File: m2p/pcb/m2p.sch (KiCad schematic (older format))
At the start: 102 parts, among them IC1 APU1205-HF-3, IC2 ADuM1201, IC3 SP100-2T, IC4 ADXL375, IC5 STM32F303C, P1 CONN_2, P2 CONN_2, P3 CONN_4, P4 CONN_2, P5 SWD, P6 CONN_2, P7 CONN_2, Q1 MOSFET_P, Q2 MOSFET_P, Q3 MOSFET_N, Q4 MOSFET_N, U1 BAT BOX, U2 ARM SW, U3 RG LED, X1 8M

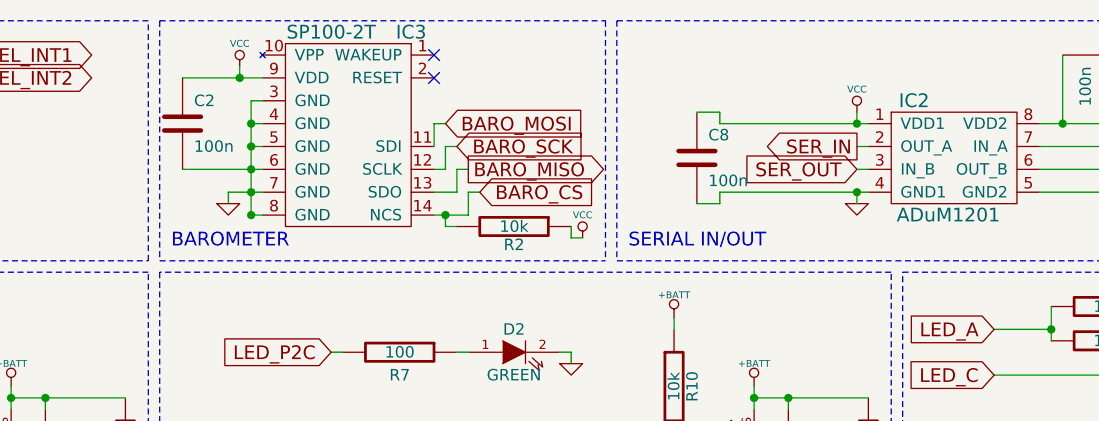
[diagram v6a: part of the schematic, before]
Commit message: swap SP100-2T for MS5611-01BA03 barometer
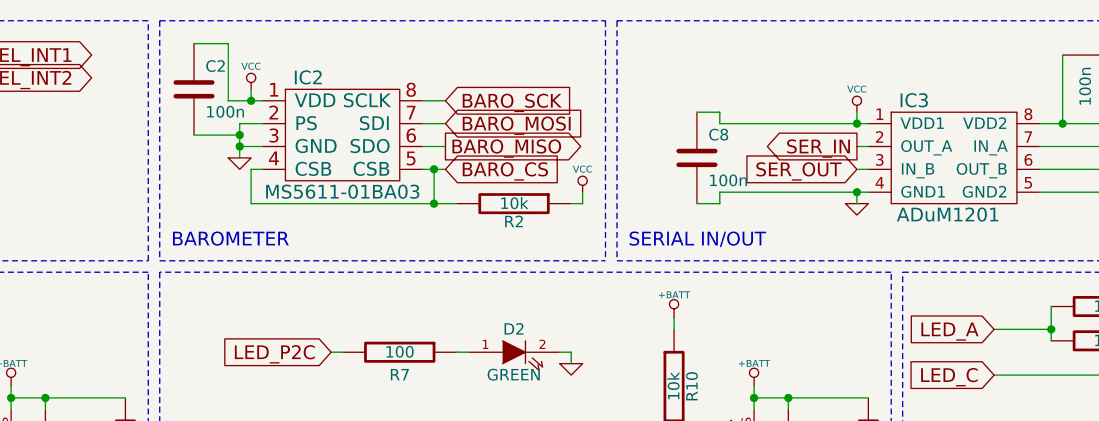
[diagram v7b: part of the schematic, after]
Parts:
- removed IC3: SP100-2T, symbol SP100-2T
- added IC2: MS5611-01BA03, symbol MS5611-01BA03
- renumbered IC2 to IC3
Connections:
- net BARO_CS: now also IC2.4 (CSB), IC2.5 (CSB)
- net BARO_MISO: now also IC2.6 (SDO)
- net BARO_MOSI: now also IC2.7 (SDI)
- net BARO_SCK: now also IC2.8 (SCLK)
- net GND: now also IC2.2 (PS), IC2.3 (GND)
- net VCC: now also IC2.1 (VDD)
- no-connect marks 11 -> 9
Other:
- moved on the sheet: C2, R2
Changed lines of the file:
@@
 LIBS:testpad
 LIBS:stm32f303c
+LIBS:ms5611-01ba03
 LIBS:m2p-cache
 EELAYER 24 0
@@
 $EndComp
 $Comp
-L VCC #PWR5
+L VCC #PWR4
 U 1 1 536844D4
 P 3200 750
-F 0 "#PWR5" H 3200 850 30  0001 C CNN
+F 0 "#PWR4" H 3200 850 30  0001 C CNN
 F 1 "VCC" H 3200 850 30  0000 C CNN
 F 2 "" H 3200 750 60  0001 C CNN
@@
 $EndComp
 $Comp
-L GND #PWR13
+L GND #PWR14
 U 1 1 536844CD
 P 3500 1250
-F 0 "#PWR13" H 3500 1250 30  0001 C CNN
+F 0 "#PWR14" H 3500 1250 30  0001 C CNN
 F 1 "GND" H 3500 1180 30  0001 C CNN
 F 2 "" H 3500 1250 60  0001 C CNN
@@
 $EndComp
 $Comp
-L VCC #PWR19
+L VCC #PWR15
 U 1 1 53683EED
-P 7950 1450
-F 0 "#PWR19" H 7950 1550 30  0001 C CNN
-F 1 "VCC" H 7950 1550 30  0000 C CNN
-F 2 "" H 7950 1450 60  0001 C CNN
-F 3 "" H 7950 1450 60  0001 C CNN
-	1    7950 1450
+P 7950 1250
+F 0 "#PWR15" H 7950 1350 30  0001 C CNN
+F 1 "VCC" H 7950 1350 30  0000 C CNN
+F 2 "" H 7950 1250 60  0001 C CNN
+F 3 "" H 7950 1250 60  0001 C CNN
+	1    7950 1250
 	1    0    0    -1
 $EndComp
@@
 L R R2
 U 1 1 53683ED0
-P 7650 1400
-F 0 "R2" V 7730 1400 50  0000 C CNN
-F 1 "10k" V 7650 1400 50  0000 C CNN
-F 2 "0603" H 7650 1400 60  0001 C CNN
-F 3 "" H 7650 1400 60  0001 C CNN
-F 4 "2332016" V 7650 1400 60  0001 C CNN "Farnell"
-	1    7650 1400
+P 7650 1300
+F 0 "R2" V 7730 1300 50  0000 C CNN
+F 1 "10k" V 7650 1300 50  0000 C CNN
+F 2 "0603" H 7650 1300 60  0001 C CNN
+F 3 "" H 7650 1300 60  0001 C CNN
+F 4 "2332016" V 7650 1300 60  0001 C CNN "Farnell"
+	1    7650 1300
 	0    1    1    0
 $EndComp
@@
 Text GLabel 4700 1150 2    60   Input ~ 0
 ACCEL_CS
-Text GLabel 7500 1250 2    60   Input ~ 0
+Text GLabel 7350 1150 2    60   Input ~ 0
 BARO_CS
-NoConn ~ 7300 750
-NoConn ~ 7300 650
-$Comp
-L VCC #PWR4
+$Comp
+L VCC #PWR5
 U 1 1 53683910
-P 6450 700
-F 0 "#PWR4" H 6450 800 30  0001 C CNN
-F 1 "VCC" H 6450 800 30  0000 C CNN
-F 2 "" H 6450 700 60  0001 C CNN
-F 3 "" H 6450 700 60  0001 C CNN
-	1    6450 700
-	1    0    0    -1
-$EndComp
-$Comp
-L GND #PWR14
+P 6500 800
+F 0 "#PWR5" H 6500 900 30  0001 C CNN
+F 1 "VCC" H 6500 900 30  0000 C CNN
+F 2 "" H 6500 800 60  0001 C CNN
+F 3 "" H 6500 800 60  0001 C CNN
+	1    6500 800
+	1    0    0    -1
+$EndComp
+$Comp
+L GND #PWR9
 U 1 1 53683901
-P 6400 1300
-F 0 "#PWR14" H 6400 1300 30  0001 C CNN
-F 1 "GND" H 6400 1230 30  0001 C CNN
-F 2 "" H 6400 1300 60  0001 C CNN
-F 3 "" H 6400 1300 60  0001 C CNN
-	1    6400 1300
+P 6450 1100
+F 0 "#PWR9" H 6450 1100 30  0001 C CNN
+F 1 "GND" H 6450 1030 30  0001 C CNN
+F 2 "" H 6450 1100 60  0001 C CNN
+F 3 "" H 6450 1100 60  0001 C CNN
+	1    6450 1100
 	1    0    0    -1
 $EndComp
 Text GLabel 7350 950  2    60   Input ~ 0
 BARO_MOSI
-Text GLabel 7400 1050 2    60   Input ~ 0
+Text GLabel 7350 850  2    60   Input ~ 0
 BARO_SCK
-Text GLabel 7450 1150 2    60   Output ~ 0
+Text GLabel 7350 1050 2    60   Output ~ 0
 BARO_MISO
 Text GLabel 4700 1350 2    60   Input ~ 0
@@
 $EndComp
 $Comp
-L GND #PWR9
+L GND #PWR10
 U 1 1 53683567
 P 3700 1150
-F 0 "#PWR9" H 3700 1150 30  0001 C CNN
+F 0 "#PWR10" H 3700 1150 30  0001 C CNN
 F 1 "GND" H 3700 1080 30  0001 C CNN
 F 2 "" H 3700 1150 60  0001 C CNN
@@
 $EndComp
 $Comp
-L GND #PWR11
+L GND #PWR12
 U 1 1 5368354F
 P 3000 1250
-F 0 "#PWR11" H 3000 1250 30  0001 C CNN
+F 0 "#PWR12" H 3000 1250 30  0001 C CNN
 F 1 "GND" H 3000 1180 30  0001 C CNN
 F 2 "" H 3000 1250 60  0001 C CNN
@@
 $EndComp
 $Comp
-L GND #PWR12
+L GND #PWR13
 U 1 1 5368353A
 P 3250 1250
-F 0 "#PWR12" H 3250 1250 30  0001 C CNN
+F 0 "#PWR13" H 3250 1250 30  0001 C CNN
 F 1 "GND" H 3250 1180 30  0001 C CNN
 F 2 "" H 3250 1250 60  0001 C CNN
@@
 $EndComp
 $Comp
-L GND #PWR10
+L GND #PWR11
 U 1 1 536834C0
 P 2600 1250
-F 0 "#PWR10" H 2600 1250 30  0001 C CNN
+F 0 "#PWR11" H 2600 1250 30  0001 C CNN
 F 1 "GND" H 2600 1180 30  0001 C CNN
 F 2 "" H 2600 1250 60  0001 C CNN
@@
 $EndComp
 $Comp
-L GND #PWR18
+L GND #PWR19
 U 1 1 536834BF
 P 2350 1450
-F 0 "#PWR18" H 2350 1450 30  0001 C CNN
+F 0 "#PWR19" H 2350 1450 30  0001 C CNN
 F 1 "GND" H 2350 1380 30  0001 C CNN
 F 2 "" H 2350 1450 60  0001 C CNN
@@
 $EndComp
 $Comp
-L GND #PWR17
+L GND #PWR18
 U 1 1 536834B9
 P 1450 1350
-F 0 "#PWR17" H 1450 1350 30  0001 C CNN
+F 0 "#PWR18" H 1450 1350 30  0001 C CNN
 F 1 "GND" H 1450 1280 30  0001 C CNN
 F 2 "" H 1450 1350 60  0001 C CNN
@@
 $EndComp
 $Comp
-L SP100-2T IC3
-U 1 1 5367F1B6
-P 6550 1350
-F 0 "IC3" H 7200 2150 60  0000 C CNN
-F 1 "SP100-2T" H 6850 2150 60  0000 C CNN
-F 2 "" H 6550 1350 60  0001 C CNN
-F 3 "" H 6550 1350 60  0001 C CNN
-F 4 "1845351" H 6550 1350 60  0001 C CNN "Farnell"
-	1    6550 1350
-	1    0    0    -1
-$EndComp
-$Comp
 L C C23
 U 1 1 5367ED56
@@
 L C C2
 U 1 1 536BD041
-P 6200 950
-F 0 "C2" H 6250 1050 50  0000 L CNN
-F 1 "100n" H 6250 850 50  0000 L CNN
-F 2 "0603" H 6200 950 60  0001 C CNN
-F 3 "" H 6200 950 60  0001 C CNN
-F 4 "1759037" H 6200 950 60  0001 C CNN "Farnell"
-	1    6200 950
+P 6250 800
+F 0 "C2" H 6300 900 50  0000 L CNN
+F 1 "100n" H 6300 700 50  0000 L CNN
+F 2 "0603" H 6250 800 60  0001 C CNN
+F 3 "" H 6250 800 60  0001 C CNN
+F 4 "1759037" H 6250 800 60  0001 C CNN "Farnell"
+	1    6250 800
 	1    0    0    -1
 $EndComp
@@
 $EndComp
 $Comp
-L GND #PWR15
+L GND #PWR16
 U 1 1 536D8EE9
 P 9150 1300
-F 0 "#PWR15" H 9150 1300 30  0001 C CNN
+F 0 "#PWR16" H 9150 1300 30  0001 C CNN
 F 1 "GND" H 9150 1230 30  0001 C CNN
 F 2 "" H 9150 1300 60  0001 C CNN
@@
 $EndComp
 $Comp
-L ADuM1201 IC2
+L ADuM1201 IC3
 U 1 1 536DA12A
 P 9550 1100
-F 0 "IC2" H 9400 1350 60  0000 C CNN
+F 0 "IC3" H 9400 1350 60  0000 C CNN
 F 1 "ADuM1201" H 9550 850 60  0000 C CNN
 F 2 "SOIC8" H 9550 1100 60  0001 C CNN
@@
 $EndComp
 $Comp
-L GND #PWR16
+L GND #PWR17
 U 1 1 537027C8
 P 600 1350
-F 0 "#PWR16" H 600 1350 30  0001 C CNN
+F 0 "#PWR17" H 600 1350 30  0001 C CNN
 F 1 "GND" H 600 1280 30  0001 C CNN
 F 2 "" H 600 1350 60  0000 C CNN
@@
 Wire Wire Line
 	1450 1300 1450 1350
-Wire Wire Line
-	6400 1250 6400 1300
-Wire Wire Line
-	6500 850  6500 1350
 Wire Notes Line
 	11150 1550 11150 500
@@
 Wire Notes Line
 	8050 500  8050 1550
-Connection ~ 6450 750
 Connection ~ 5600 2650
 Wire Wire Line
@@
 Wire Wire Line
 	3500 1200 3500 1250
-Wire Wire Line
-	7900 1450 7950 1450
-Wire Wire Line
-	7900 1400 7900 1450
-Connection ~ 7350 1350
-Wire Wire Line
-	7350 1400 7350 1350
-Wire Wire Line
-	7450 1250 7500 1250
-Wire Wire Line
-	7450 1350 7450 1250
-Wire Wire Line
-	7300 1350 7450 1350
-Wire Wire Line
-	7350 1050 7400 1050
-Wire Wire Line
-	7350 1150 7350 1050
-Wire Wire Line
-	7300 1150 7350 1150
 Connection ~ 4600 1150
 Wire Wire Line
@@
 Wire Notes Line
 	6100 500  6100 1550
-Wire Wire Line
-	6450 750  6450 700
-Wire Wire Line
-	6200 750  6550 750
-Connection ~ 6500 1050
-Wire Wire Line
-	6500 950  6550 950
-Connection ~ 6500 1250
-Wire Wire Line
-	6200 1150 6550 1150
-Wire Wire Line
-	6500 1350 6550 1350
 Wire Wire Line
 	1100 7400 1100 7450
@@
 Wire Wire Line
 	1100 6750 1100 6700
-Wire Wire Line
-	6400 1250 6550 1250
-Connection ~ 6500 1350
-Wire Wire Line
-	6500 1050 6550 1050
-Connection ~ 6500 1150
-Wire Wire Line
-	6500 850  6550 850
-Connection ~ 6500 950
 Wire Notes Line
 	2850 500  2850 1550
@@
 Wire Wire Line
 	5100 900  5100 950
-Wire Wire Line
-	7300 950  7300 1050
-Wire Wire Line
-	7350 950  7300 950
-Wire Wire Line
-	7400 1250 7300 1250
-Wire Wire Line
-	7400 1150 7400 1250
-Wire Wire Line
-	7450 1150 7400 1150
-Wire Wire Line
-	7400 1400 7350 1400
 Wire Notes Line
 	6100 500  8050 500
@@
 	1    0    0    -1
 $EndComp
+$Comp
+L MS5611-01BA03 IC2
+U 1 1 5387D30F
+P 6900 950
+F 0 "IC2" H 6750 1150 60  0000 C CNN
+F 1 "MS5611-01BA03" H 6900 650 60  0000 C CNN
+F 2 "" H 6900 950 60  0000 C CNN
+F 3 "" H 6900 950 60  0000 C CNN
+	1    6900 950
+	1    0    0    -1
+$EndComp
+Wire Wire Line
+	6550 1050 6450 1050
+Wire Wire Line
+	6450 950  6450 1100
+Wire Wire Line
+	6550 950  6450 950
+Connection ~ 6450 1050
+Wire Wire Line
+	6250 1000 6450 1000
+Connection ~ 6450 1000
+Wire Wire Line
+	6400 850  6550 850
+Wire Wire Line
+	6500 850  6500 800
+Wire Wire Line
+	6250 600  6400 600
+Wire Wire Line
+	6400 600  6400 850
+Connection ~ 6500 850
+Wire Wire Line
+	7250 850  7350 850
+Wire Wire Line
+	7250 950  7350 950
+Wire Wire Line
+	7250 1050 7350 1050
+Wire Wire Line
+	7250 1150 7350 1150
+Wire Wire Line
+	6550 1150 6500 1150
+Wire Wire Line
+	6500 1150 6500 1300
+Wire Wire Line
+	6500 1300 7400 1300
+Wire Wire Line
+	7300 1300 7300 1150
+Connection ~ 7300 1150
+Connection ~ 7300 1300
+Wire Wire Line
+	7900 1300 7950 1300
+Wire Wire Line
+	7950 1300 7950 1250
 $EndSCHEMATC

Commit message: add farnell number for new barometer
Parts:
- IC2: Farnell (none) -> 2362662
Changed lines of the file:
@@
 F 2 "" H 6900 950 60  0000 C CNN
 F 3 "" H 6900 950 60  0000 C CNN
+F 4 "2362662" H 6900 950 60  0001 C CNN "Farnell"
 	1    6900 950
 	1    0    0    -1
